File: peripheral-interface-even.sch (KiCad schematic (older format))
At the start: 5 parts

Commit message: Fix wiring in root sheet
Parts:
- removed J?: Conn_01x08, symbol Connector_Generic:Conn_01x08
- added J?: Conn_01x08, symbol Connector_Generic:Conn_01x08
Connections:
- net at U?.18 (PB0): now also J?.1 (Pin_1)
- net at U?.19 (PB1): now also J?.2 (Pin_2)
- net at U?.20 (PB2): now also J?.3 (Pin_3)
- net at U?.21 (PB3): now also J?.4 (Pin_4)
- net at U?.22 (PB4): now also J?.5 (Pin_5)
- net at U?.23 (PB5): now also J?.6 (Pin_6)
- net at U?.24 (PB6): now also J?.7 (Pin_7)
- net at U?.25 (PB7): now also J?.8 (Pin_8)
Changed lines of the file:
@@
 $Descr A4 11693 8268
 encoding utf-8
-Sheet 11 14
+Sheet 11 15
 Title "Peripheral Interface"
 Date ""
@@
 $Comp
 L Connector_Generic:Conn_01x08 J?
-U 1 1 61C3EA07
+U 1 1 61ABA7C2
 P 5900 3575
-AR Path="/61BFC8AC/61C0115A/61C3EA07" Ref="J?"  Part="1"
-AR Path="/61BFC8AC/61C2038B/61C3EA07" Ref="J?"  Part="1"
-AR Path="/61BFC8AC/61C20895/61C3EA07" Ref="J?"  Part="1"
-AR Path="/61C40B21/61C3EA07" Ref="J?"  Part="1"
-AR Path="/61C417C6/61C3EA07" Ref="J?"  Part="1"
-AR Path="/61C41B68/61C3EA07" Ref="J?"  Part="1"
+AR Path="/61BFC8AC/61C0115A/61ABA7C2" Ref="J?"  Part="1"
+AR Path="/61BFC8AC/61C2038B/61ABA7C2" Ref="J?"  Part="1"
+AR Path="/61BFC8AC/61C20895/61ABA7C2" Ref="J?"  Part="1"
+AR Path="/61C40B21/61ABA7C2" Ref="J?"  Part="1"
+AR Path="/61C417C6/61ABA7C2" Ref="J?"  Part="1"
+AR Path="/61C41B68/61ABA7C2" Ref="J?"  Part="1"
 F 0 "J?" H 5980 3567 50  0000 L CNN
 F 1 "Conn_01x08" H 5980 3476 50  0000 L CNN
@@
 $Comp
 L power:GND #PWR?
-U 1 1 61C61024
+U 1 1 61ABA7C6
 P 7875 3525
-AR Path="/61C417C6/61C61024" Ref="#PWR?"  Part="1"
-AR Path="/61C41B68/61C61024" Ref="#PWR?"  Part="1"
-AR Path="/61C40B21/61C61024" Ref="#PWR?"  Part="1"
+AR Path="/61C417C6/61ABA7C6" Ref="#PWR?"  Part="1"
+AR Path="/61C41B68/61ABA7C6" Ref="#PWR?"  Part="1"
+AR Path="/61C40B21/61ABA7C6" Ref="#PWR?"  Part="1"
 F 0 "#PWR?" H 7875 3275 50  0001 C CNN
 F 1 "GND" H 7880 3352 50  0000 C CNN

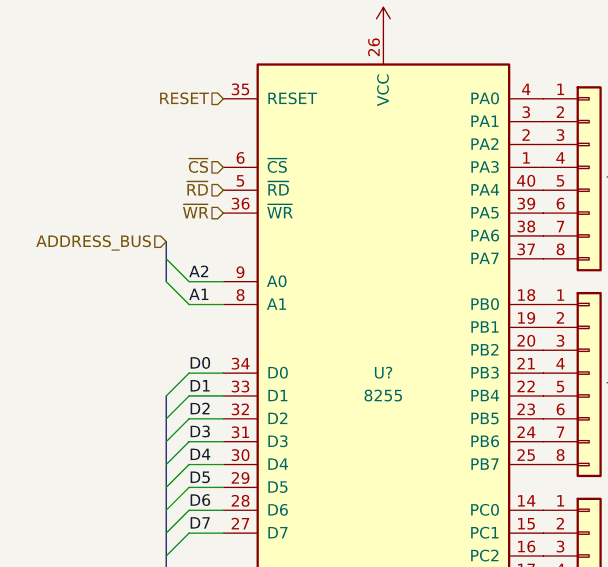
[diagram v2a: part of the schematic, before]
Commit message: General edits; removed floating inputs
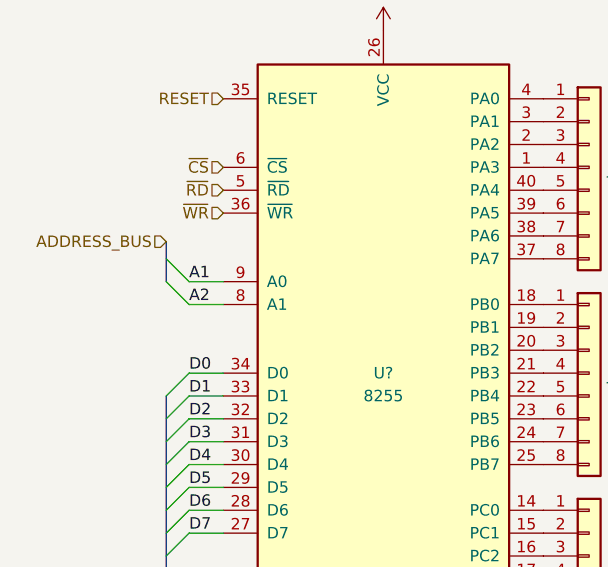
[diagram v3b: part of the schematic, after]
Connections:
- net A1: now also U?.9 (A0); no longer U?.8 (A1)
- net A2: now also U?.8 (A1); no longer U?.9 (A0)
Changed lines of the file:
@@
 $Descr A4 11693 8268
 encoding utf-8
-Sheet 11 15
+Sheet 8 15
 Title "Peripheral Interface"
 Date ""
@@
 	4050 3075 4150 3175
 Text Label 4150 3275 0    50   ~ 0
+A2
+Text Label 4150 3175 0    50   ~ 0
 A1
-Text Label 4150 3175 0    50   ~ 0
-A2
 Wire Wire Line
 	4300 3175 4150 3175

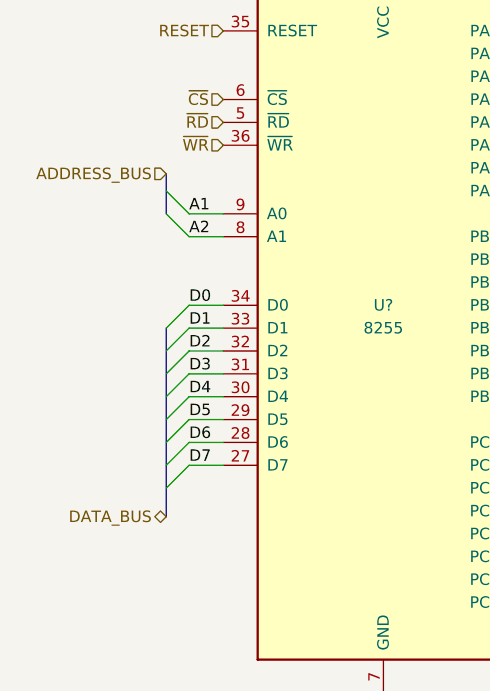
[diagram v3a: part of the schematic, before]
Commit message: Updates to pass ERC
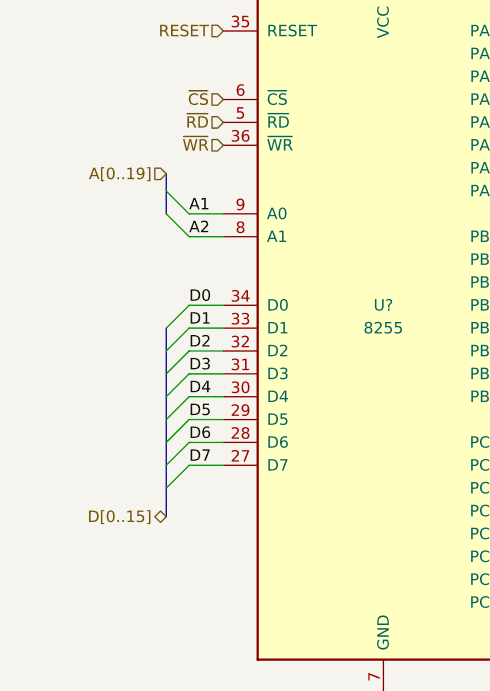
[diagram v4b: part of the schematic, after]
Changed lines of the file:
@@
 $EndComp
 Text HLabel 4050 3000 0    50   Input ~ 0
-ADDRESS_BUS
+A[0..19]
 Entry Wire Line
 	4050 3175 4150 3275
@@
 $EndComp
 Text HLabel 4050 4500 0    50   BiDi ~ 0
-DATA_BUS
+D[0..15]
 Entry Wire Line
 	4050 4375 4150 4275

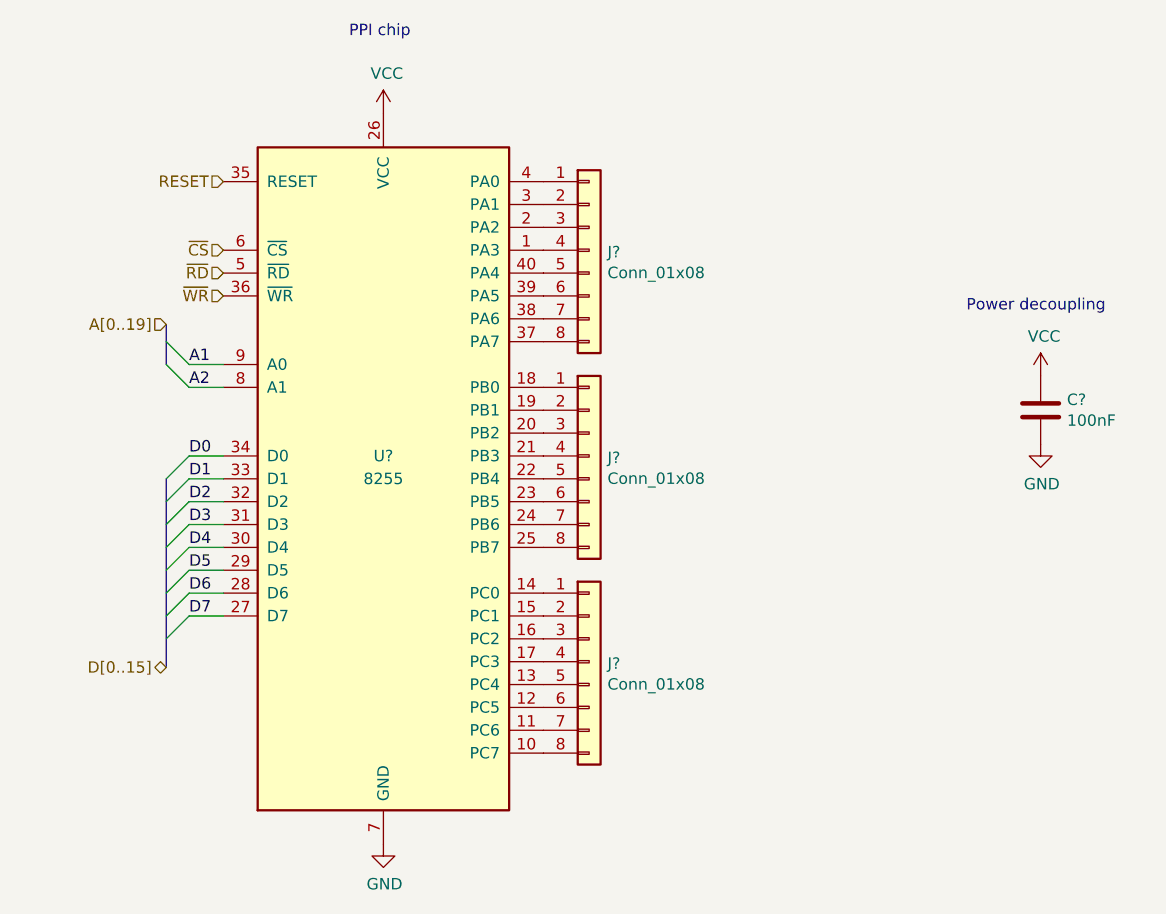
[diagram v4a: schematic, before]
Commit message: Assign footprints for most symbols
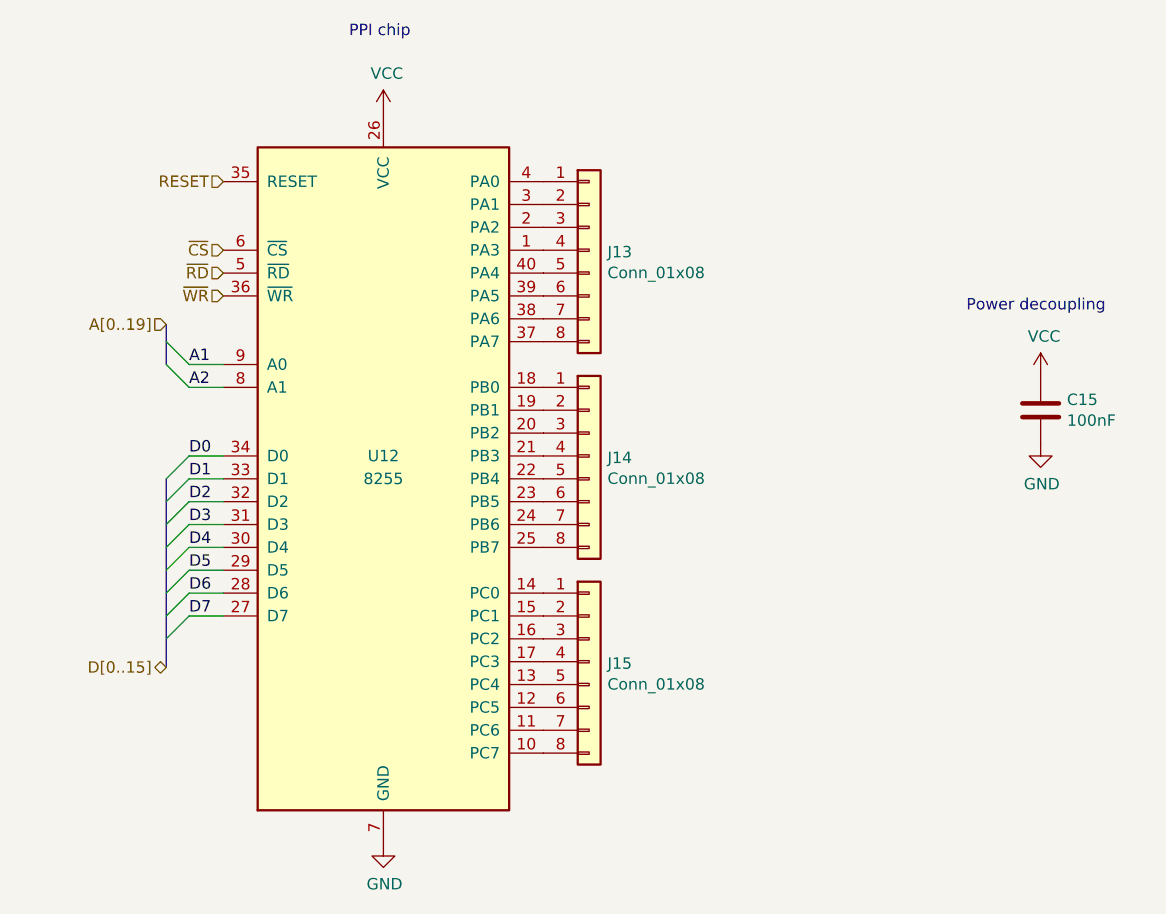
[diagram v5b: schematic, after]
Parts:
- C15: renamed from C?; footprint (none) -> Capacitor_THT:C_Rect_L4.0mm_W2.5mm_P2.50mm
- J13, J14: renamed from J?; footprint (none) -> Connector_PinHeader_2.54mm:PinHeader_1x08_P2.54mm_Vertical
- J15: renamed from J?; footprint (none) -> Connector_PinHeader_2.54mm:PinHeader_1x03_P2.54mm_Vertical
- gave numbers to parts that had none: 1
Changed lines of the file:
@@
 AR Path="/61BFC8AC/61C20895/61C3F083" Ref="J?"  Part="1"
 AR Path="/61C40B21/61C3F083" Ref="J?"  Part="1"
-AR Path="/61C417C6/61C3F083" Ref="J?"  Part="1"
+AR Path="/61C417C6/61C3F083" Ref="J15"  Part="1"
 AR Path="/61C41B68/61C3F083" Ref="J?"  Part="1"
-F 0 "J?" H 5980 4467 50  0000 L CNN
+F 0 "J15" H 5980 4467 50  0000 L CNN
 F 1 "Conn_01x08" H 5980 4376 50  0000 L CNN
-F 2 "" H 5900 4475 50  0001 C CNN
+F 2 "Connector_PinHeader_2.54mm:PinHeader_1x03_P2.54mm_Vertical" H 5900 4475 50  0001 C CNN
 F 3 "~" H 5900 4475 50  0001 C CNN
 	1    5900 4475
@@
 AR Path="/61BFC8AC/61C20895/61ABA7C2" Ref="J?"  Part="1"
 AR Path="/61C40B21/61ABA7C2" Ref="J?"  Part="1"
-AR Path="/61C417C6/61ABA7C2" Ref="J?"  Part="1"
+AR Path="/61C417C6/61ABA7C2" Ref="J14"  Part="1"
 AR Path="/61C41B68/61ABA7C2" Ref="J?"  Part="1"
-F 0 "J?" H 5980 3567 50  0000 L CNN
+F 0 "J14" H 5980 3567 50  0000 L CNN
 F 1 "Conn_01x08" H 5980 3476 50  0000 L CNN
-F 2 "" H 5900 3575 50  0001 C CNN
+F 2 "Connector_PinHeader_2.54mm:PinHeader_1x08_P2.54mm_Vertical" H 5900 3575 50  0001 C CNN
 F 3 "~" H 5900 3575 50  0001 C CNN
 	1    5900 3575
@@
 AR Path="/61BFC8AC/61C20895/61C397EF" Ref="J?"  Part="1"
 AR Path="/61C40B21/61C397EF" Ref="J?"  Part="1"
-AR Path="/61C417C6/61C397EF" Ref="J?"  Part="1"
+AR Path="/61C417C6/61C397EF" Ref="J13"  Part="1"
 AR Path="/61C41B68/61C397EF" Ref="J?"  Part="1"
-F 0 "J?" H 5980 2667 50  0000 L CNN
+F 0 "J13" H 5980 2667 50  0000 L CNN
 F 1 "Conn_01x08" H 5980 2576 50  0000 L CNN
-F 2 "" H 5900 2675 50  0001 C CNN
+F 2 "Connector_PinHeader_2.54mm:PinHeader_1x08_P2.54mm_Vertical" H 5900 2675 50  0001 C CNN
 F 3 "~" H 5900 2675 50  0001 C CNN
 	1    5900 2675
@@
 AR Path="/61BFC8AC/61C20895/61C2D896" Ref="#PWR?"  Part="1"
 AR Path="/61C40B21/61C2D896" Ref="#PWR?"  Part="1"
-AR Path="/61C417C6/61C2D896" Ref="#PWR?"  Part="1"
+AR Path="/61C417C6/61C2D896" Ref="#PWR0147"  Part="1"
 AR Path="/61C41B68/61C2D896" Ref="#PWR?"  Part="1"
-F 0 "#PWR?" H 5000 5025 50  0001 C CNN
+F 0 "#PWR0147" H 5000 5025 50  0001 C CNN
 F 1 "GND" H 5005 5102 50  0000 C CNN
 F 2 "" H 5000 5275 50  0001 C CNN
@@
 AR Path="/61BFC8AC/61C20895/61C2CF0A" Ref="#PWR?"  Part="1"
 AR Path="/61C40B21/61C2CF0A" Ref="#PWR?"  Part="1"
-AR Path="/61C417C6/61C2CF0A" Ref="#PWR?"  Part="1"
+AR Path="/61C417C6/61C2CF0A" Ref="#PWR0148"  Part="1"
 AR Path="/61C41B68/61C2CF0A" Ref="#PWR?"  Part="1"
-F 0 "#PWR?" H 5000 1925 50  0001 C CNN
+F 0 "#PWR0148" H 5000 1925 50  0001 C CNN
 F 1 "VCC" H 5015 2248 50  0000 C CNN
 F 2 "" H 5000 2075 50  0001 C CNN
@@
 AR Path="/61BFC8AC/61C20AEA/61C013ED" Ref="U?"  Part="1"
 AR Path="/61C40B21/61C013ED" Ref="U?"  Part="1"
-AR Path="/61C417C6/61C013ED" Ref="U?"  Part="1"
+AR Path="/61C417C6/61C013ED" Ref="U12"  Part="1"
 AR Path="/61C41B68/61C013ED" Ref="U?"  Part="1"
-F 0 "U?" H 5000 3775 50  0000 C CNN
+F 0 "U12" H 5000 3775 50  0000 C CNN
 F 1 "8255" H 5000 3675 50  0000 C CNN
 F 2 "Package_DIP:DIP-40_W15.24mm" H 5000 3975 50  0001 C CNN
@@
 PPI chip
 $Comp
-L Device:C C?
+L Device:C C15
 U 1 1 61C5D8E9
 P 7875 3375
-AR Path="/61C417C6/61C5D8E9" Ref="C?"  Part="1"
+AR Path="/61C417C6/61C5D8E9" Ref="C15"  Part="1"
 AR Path="/61C41B68/61C5D8E9" Ref="C?"  Part="1"
 AR Path="/61C40B21/61C5D8E9" Ref="C?"  Part="1"
-F 0 "C?" H 7990 3421 50  0000 L CNN
+F 0 "C15" H 7990 3421 50  0000 L CNN
 F 1 "100nF" H 7990 3330 50  0000 L CNN
-F 2 "" H 7913 3225 50  0001 C CNN
+F 2 "Capacitor_THT:C_Rect_L4.0mm_W2.5mm_P2.50mm" H 7913 3225 50  0001 C CNN
 F 3 "~" H 7875 3375 50  0001 C CNN
 	1    7875 3375
@@
 $EndComp
 $Comp
-L power:VCC #PWR?
+L power:VCC #PWR0149
 U 1 1 61C60AFC
 P 7875 3225
-AR Path="/61C417C6/61C60AFC" Ref="#PWR?"  Part="1"
+AR Path="/61C417C6/61C60AFC" Ref="#PWR0149"  Part="1"
 AR Path="/61C41B68/61C60AFC" Ref="#PWR?"  Part="1"
 AR Path="/61C40B21/61C60AFC" Ref="#PWR?"  Part="1"
-F 0 "#PWR?" H 7875 3075 50  0001 C CNN
+F 0 "#PWR0149" H 7875 3075 50  0001 C CNN
 F 1 "VCC" H 7890 3398 50  0000 C CNN
 F 2 "" H 7875 3225 50  0001 C CNN
@@
 $EndComp
 $Comp
-L power:GND #PWR?
+L power:GND #PWR0150
 U 1 1 61ABA7C6
 P 7875 3525
-AR Path="/61C417C6/61ABA7C6" Ref="#PWR?"  Part="1"
+AR Path="/61C417C6/61ABA7C6" Ref="#PWR0150"  Part="1"
 AR Path="/61C41B68/61ABA7C6" Ref="#PWR?"  Part="1"
 AR Path="/61C40B21/61ABA7C6" Ref="#PWR?"  Part="1"
-F 0 "#PWR?" H 7875 3275 50  0001 C CNN
+F 0 "#PWR0150" H 7875 3275 50  0001 C CNN
 F 1 "GND" H 7880 3352 50  0000 C CNN
 F 2 "" H 7875 3525 50  0001 C CNN

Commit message: begin pcb layout
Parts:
- J13: value Conn_01x08 -> PORT A
- J14: value Conn_01x08 -> PORT B
- J15: value Conn_01x08 -> PORT C; footprint Connector_PinHeader_2.54mm:PinHeader_1x03_P2.54mm_Vertical -> Connector_PinHeader_2.54mm:PinHeader_1x08_P2.54mm_Vertical
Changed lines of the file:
@@
 AR Path="/61C41B68/61C3F083" Ref="J?"  Part="1"
 F 0 "J15" H 5980 4467 50  0000 L CNN
-F 1 "Conn_01x08" H 5980 4376 50  0000 L CNN
-F 2 "Connector_PinHeader_2.54mm:PinHeader_1x03_P2.54mm_Vertical" H 5900 4475 50  0001 C CNN
+F 1 "PORT C" H 5980 4376 50  0000 L CNN
+F 2 "Connector_PinHeader_2.54mm:PinHeader_1x08_P2.54mm_Vertical" H 5900 4475 50  0001 C CNN
 F 3 "~" H 5900 4475 50  0001 C CNN
 	1    5900 4475
@@
 AR Path="/61C41B68/61ABA7C2" Ref="J?"  Part="1"
 F 0 "J14" H 5980 3567 50  0000 L CNN
-F 1 "Conn_01x08" H 5980 3476 50  0000 L CNN
+F 1 "PORT B" H 5980 3476 50  0000 L CNN
 F 2 "Connector_PinHeader_2.54mm:PinHeader_1x08_P2.54mm_Vertical" H 5900 3575 50  0001 C CNN
 F 3 "~" H 5900 3575 50  0001 C CNN
@@
 AR Path="/61C41B68/61C397EF" Ref="J?"  Part="1"
 F 0 "J13" H 5980 2667 50  0000 L CNN
-F 1 "Conn_01x08" H 5980 2576 50  0000 L CNN
+F 1 "PORT A" H 5980 2576 50  0000 L CNN
 F 2 "Connector_PinHeader_2.54mm:PinHeader_1x08_P2.54mm_Vertical" H 5900 2675 50  0001 C CNN
 F 3 "~" H 5900 2675 50  0001 C CNN
